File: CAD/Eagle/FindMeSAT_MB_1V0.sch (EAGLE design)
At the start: 107 parts, among them IC1111 LM2831YMF, J291 MCX-J-P-X-RA-SM1, J701 MOLEX_105017-0001, J801 MICROSIM-8P_SDCARD-8P_MOLEX-1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, J901 JST_S3B-XH-A, Q101 ABS07, U1001 CFPT-141, U101 ATXMEGA256A3BU-AU, U1011 OPA354, U1021 OPA354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

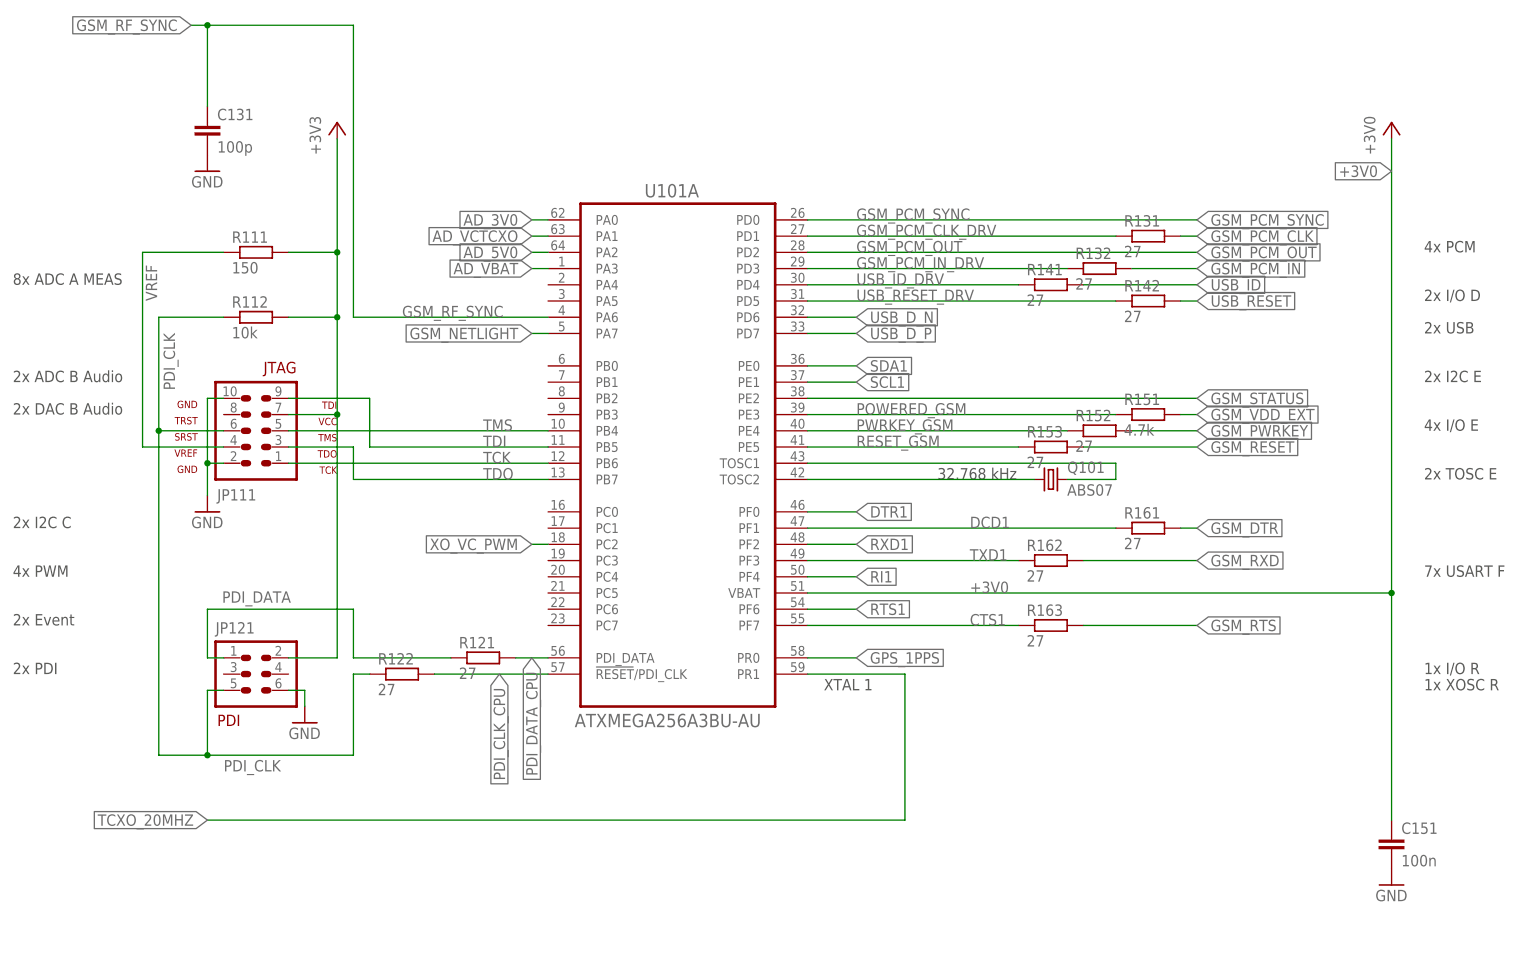
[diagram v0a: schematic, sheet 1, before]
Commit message: Eagle - missing Display header added
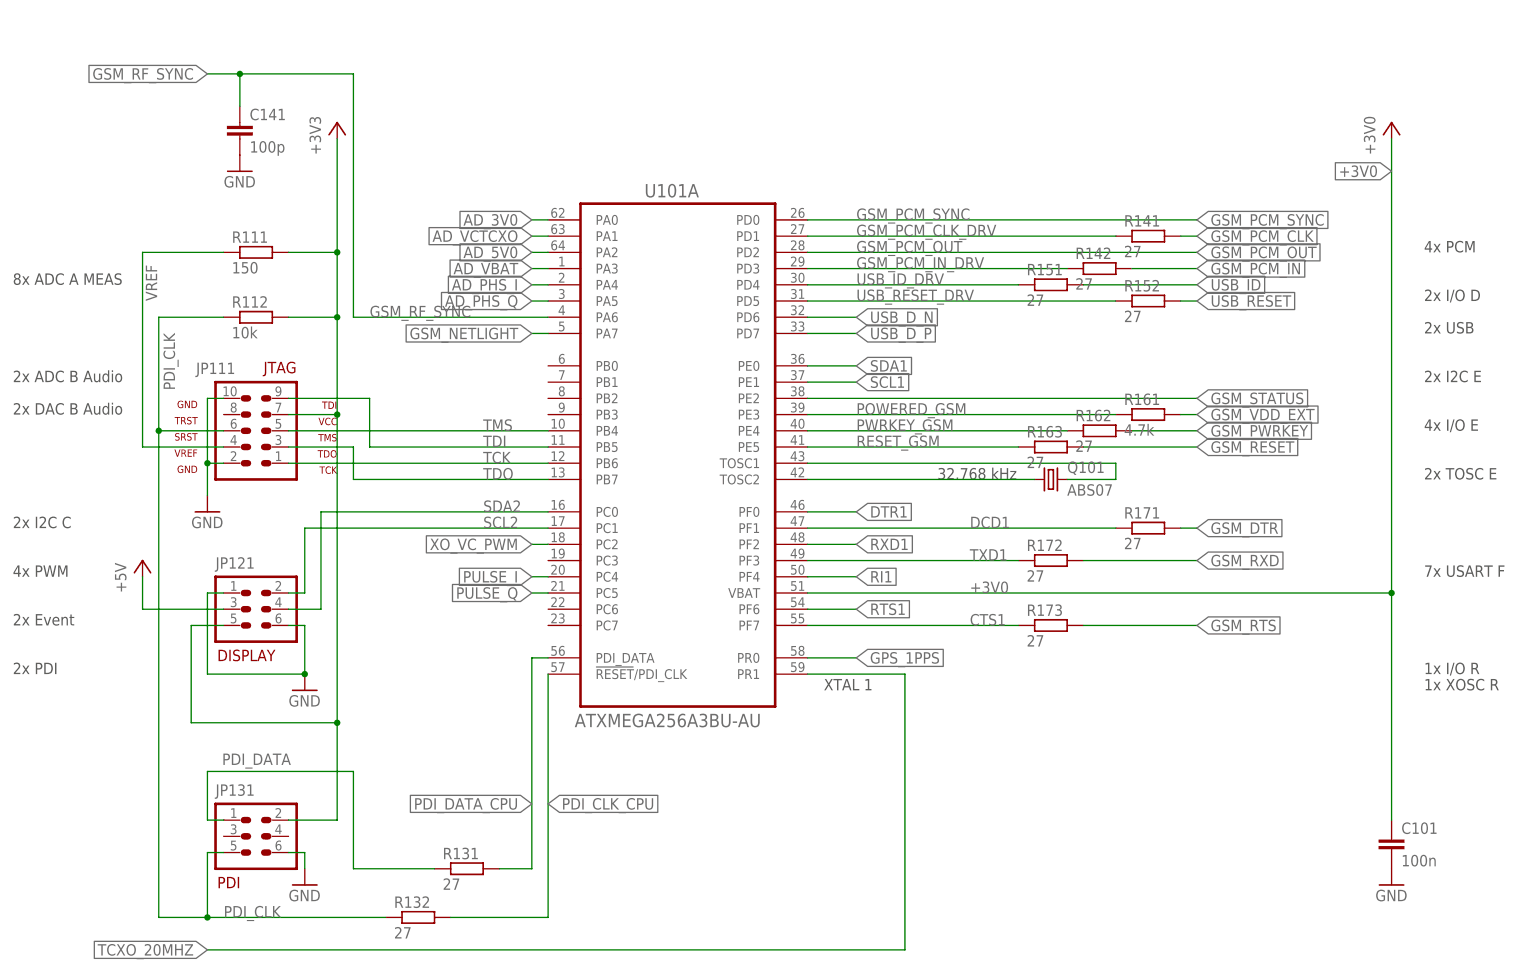
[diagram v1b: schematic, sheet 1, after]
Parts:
- removed C131: 100p, rcl:C-EUC0603
- removed R121, R122, R153: 27, rcl:R-EU_R0603
- added C141: 100p, rcl:C-EUC0603
- added JP131: PDI, df4iah_connector:HEADER-2X3
- added R171, R172, R173: 27, rcl:R-EU_R0603
- JP121: value PDI -> DISPLAY
- R151: value 4.7k -> 27
- R161: value 27 -> 4.7k
- renumbered C151 to C101
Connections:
- new net AD_PHS_I: U101A.PA4
- new net AD_PHS_Q: U101A.PA5
- new net PULSE_I: U101A.PC4
- new net PULSE_Q: U101A.PC5
- new net SCL2: JP121.2, U101A.PC1
- new net SDA2: JP121.4, U101A.PC0
- net +3V3: now also JP121.5, JP131.2; no longer JP121.2
- net +5V: now also JP121.3
- net CTS1: now also R173.1; no longer R163.1
- net DCD1: now also R171.1; no longer R161.1
- net GND: now also C141.2, JP121.1, JP131.6; no longer C131.2
- net GSM_DTR: now also R171.2; no longer R161.2
- net GSM_PCM_CLK: now also R141.2; no longer R131.2
- net GSM_PCM_CLK_DRV: now also R141.1; no longer R131.1
- net GSM_PCM_IN: now also R142.2; no longer R132.2
- net GSM_PCM_IN_DRV: now also R142.1; no longer R132.1
- net GSM_PWRKEY: now also R162.2; no longer R152.2
- net GSM_RESET: now also R163.2; no longer R153.2
- net GSM_RF_SYNC: now also C141.1; no longer C131.1
- net GSM_RTS: now also R173.2; no longer R163.2
- net GSM_RXD: now also R172.2; no longer R162.2
- net GSM_VDD_EXT: now also R161.2; no longer R151.2
- net PDI_CLK: now also JP131.5, R132.1; no longer JP121.5, R122.1
- net PDI_CLK_CPU: now also R132.2; no longer R122.2
- net PDI_DATA: now also JP131.1, R131.1; no longer JP121.1, R121.1
- net PDI_DATA_CPU: now also R131.2; no longer R121.2
- net POWERED_GSM: now also R161.1; no longer R151.1
- net PWRKEY_GSM: now also R162.1; no longer R152.1
- net RESET_GSM: now also R163.1; no longer R153.1
- net TXD1: now also R172.1; no longer R162.1
- net USB_ID: now also R151.2; no longer R141.2
- net USB_ID_DRV: now also R151.1; no longer R141.1
- net USB_RESET: now also R152.2; no longer R142.2
- net USB_RESET_DRV: now also R152.1; no longer R142.1
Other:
- note added: "DISPLAY"
- moved on the sheet: JP121, R131, R132, R141, R142, R151, R152, R161, R162, R163

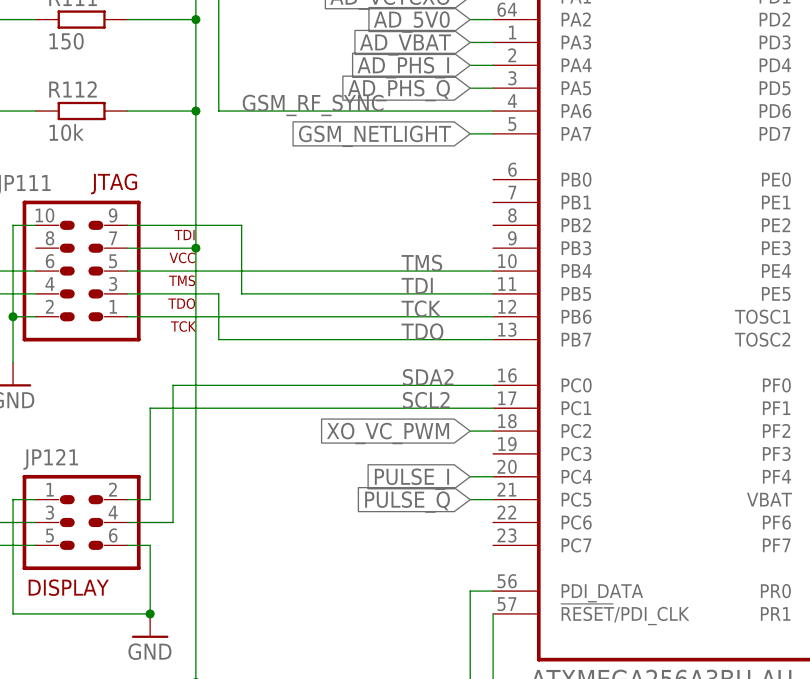
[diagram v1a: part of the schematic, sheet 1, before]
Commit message: Eagle - additional sensors added (9-axis: accel / gyro / magneto, baro, hygro)
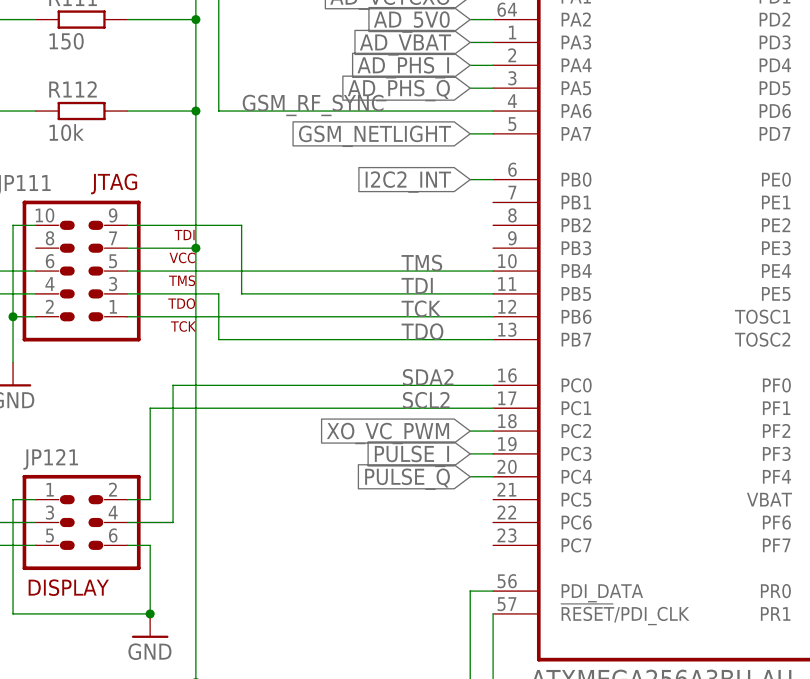
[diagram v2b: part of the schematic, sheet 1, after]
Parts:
- added C301, C302, C401, C501: 100n, rcl:C-EUC0603
- added U301: MPU-9250, df4iah_sensors:MPU-9250
- added U401: BMP180, df4iah_sensors:BMP180
- added U501: SHT31-DIS, df4iah_sensors:SHT31-DIS
- U101: device df4iah_mmu:ATXMEGA256A3BU-AU -> df4iah_processors:ATXMEGA256A3BU-AU
- U201: device adafruit:GSM_SIM808_LITERAL -> df4iah_processors:SIM808
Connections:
- new net GAM_RO: C302.1, U301.REGOUT
- new net I2C2_INT: U101A.PB0, U301.INT
- net +3V3: now also C301.1, C401.1, C501.1, U301.!CS, U301.VDD, U301.VDDIO, U401.VDD, U401.VDDIO, U501.VDD
- net GND: now also C301.2, C302.2, C401.2, C501.2, U301.AD0/SDO, U301.FSYNC, U301.GND, U401.GND, U501.ADDR, U501.PAD, U501.R, U501.VSS
- net PULSE_I: now also U101A.PC3; no longer U101A.PC4
- net PULSE_Q: now also U101A.PC4; no longer U101A.PC5
- net SCL1: now also U301.SCL/SCLK, U401.SCL, U501.SCL
- net SDA1: now also U301.SDA/SDI, U401.SDA, U501.SDA
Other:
- note added: "I2C address = 1000100"
- note added: "I2C address = 1101000"
- note added: "I2C address = 1110111"
- note added: "NC"

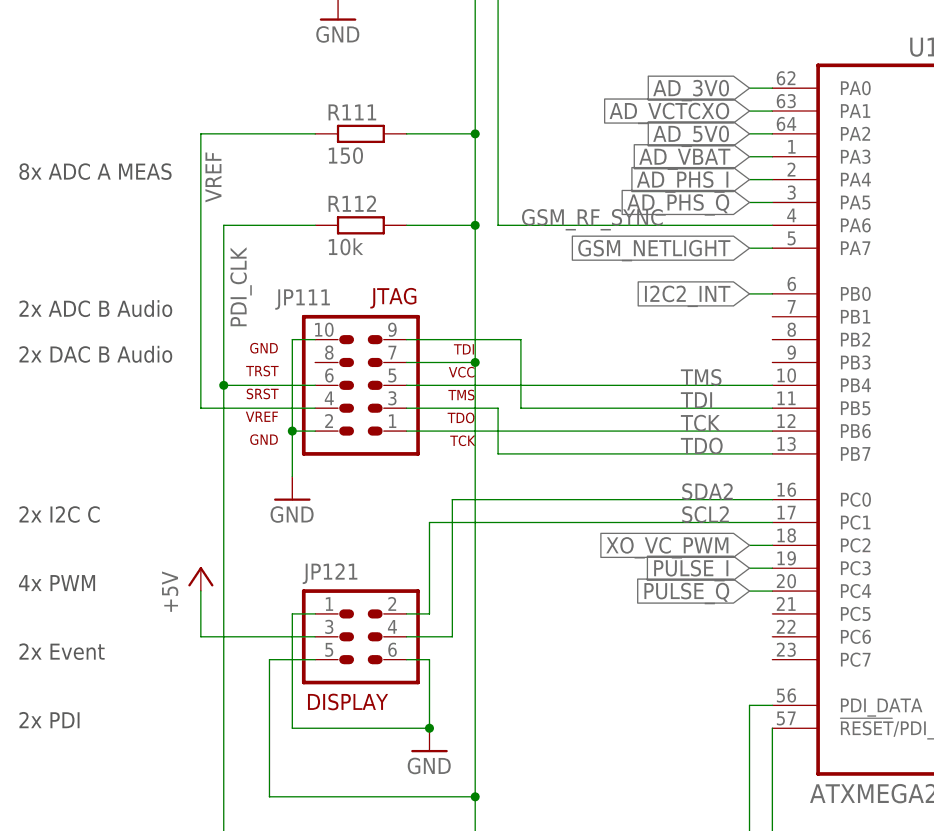
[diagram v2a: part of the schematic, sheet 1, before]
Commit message: Eagle - AX5243 included and library works done
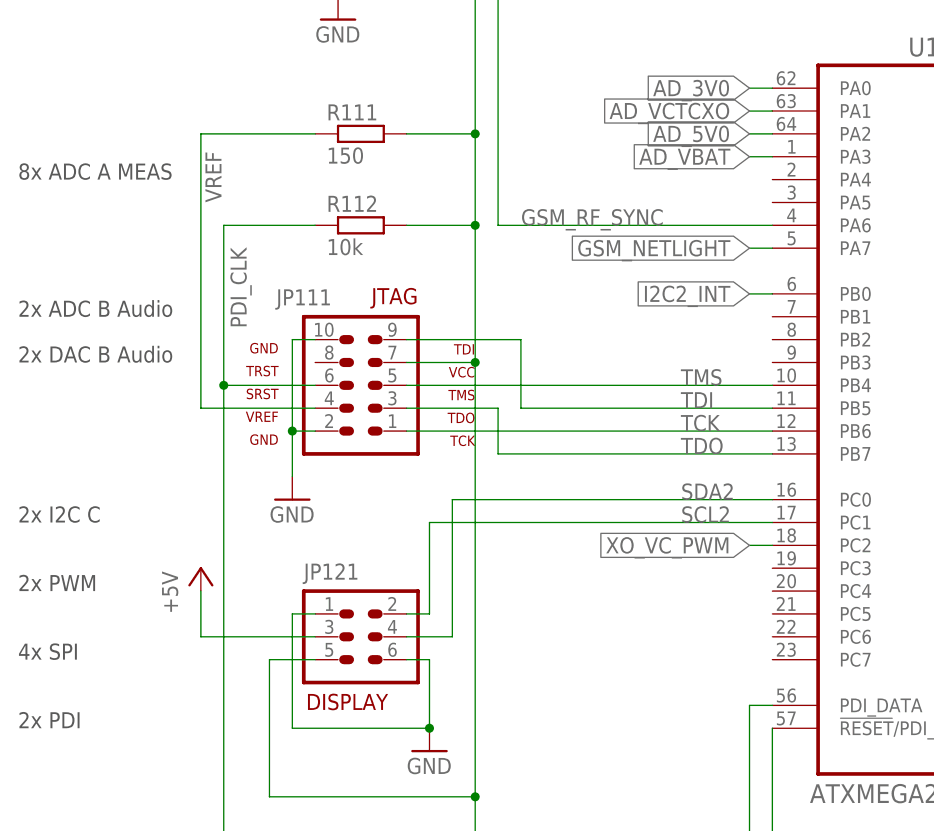
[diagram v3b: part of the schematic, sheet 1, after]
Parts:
- added C601: 47u, rcl:C-EUC0603
- added C602, C611, C612: 100n, rcl:C-EUC0603
- added L671: 22nH, rcl:R-EU_R0603
- added Q651: ABM3B-16MHZ-10-R50-1-U, adafruit:CRYSTALCTS406
- added R621: 27, rcl:R-EU_R0603
- added R631: 10k, rcl:R-EU_R0603
- added U601: AX5243, df4iah_rf:AX5243
- U201: device df4iah_processors:SIM808 -> df4iah_gsm:SIM808
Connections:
- removed net AD_PHS_I: U101A.PA4
- removed net AD_PHS_Q: U101A.PA5
- removed net PULSE_I: U101A.PC3
- removed net PULSE_Q: U101A.PC4
- new net AX_CLK: U601.CLK
- new net AX_IRQ: R631.1, U601.IRQ
- new net AX_L1: L671.1, U601.L1
- new net AX_L2: L671.2, U601.L2
- new net AX_MISO: R621.2, U601.MISO
- new net AX_MOSI: U601.MOSI
- new net AX_SEL: U601.SEL
- new net CLK16N: Q651.1, U601.CLK16N
- new net CLK16P: Q651.2, U601.CLK16P
- new net N$1: C611.1, U601.VDD_ANA@1
- new net SPI_MISO: R621.1
- new net VDD_ANA@5: C612.1, U601.VDD_ANA@5
- net +3V3: now also C601.1, C602.1
- net GND: now also C601.2, C602.2, C611.2, C612.2, U601.GND, U601.GPADC1, U601.GPADC2
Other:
- note added: "2x PWM"
- note added: "4x SPI"
- note added: "Transistor needed"
- note removed: "2x Event"
- note removed: "4x PWM"
